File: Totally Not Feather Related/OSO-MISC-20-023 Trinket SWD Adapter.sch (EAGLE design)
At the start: 5 parts, among them X2 2x5 0.05" SWD

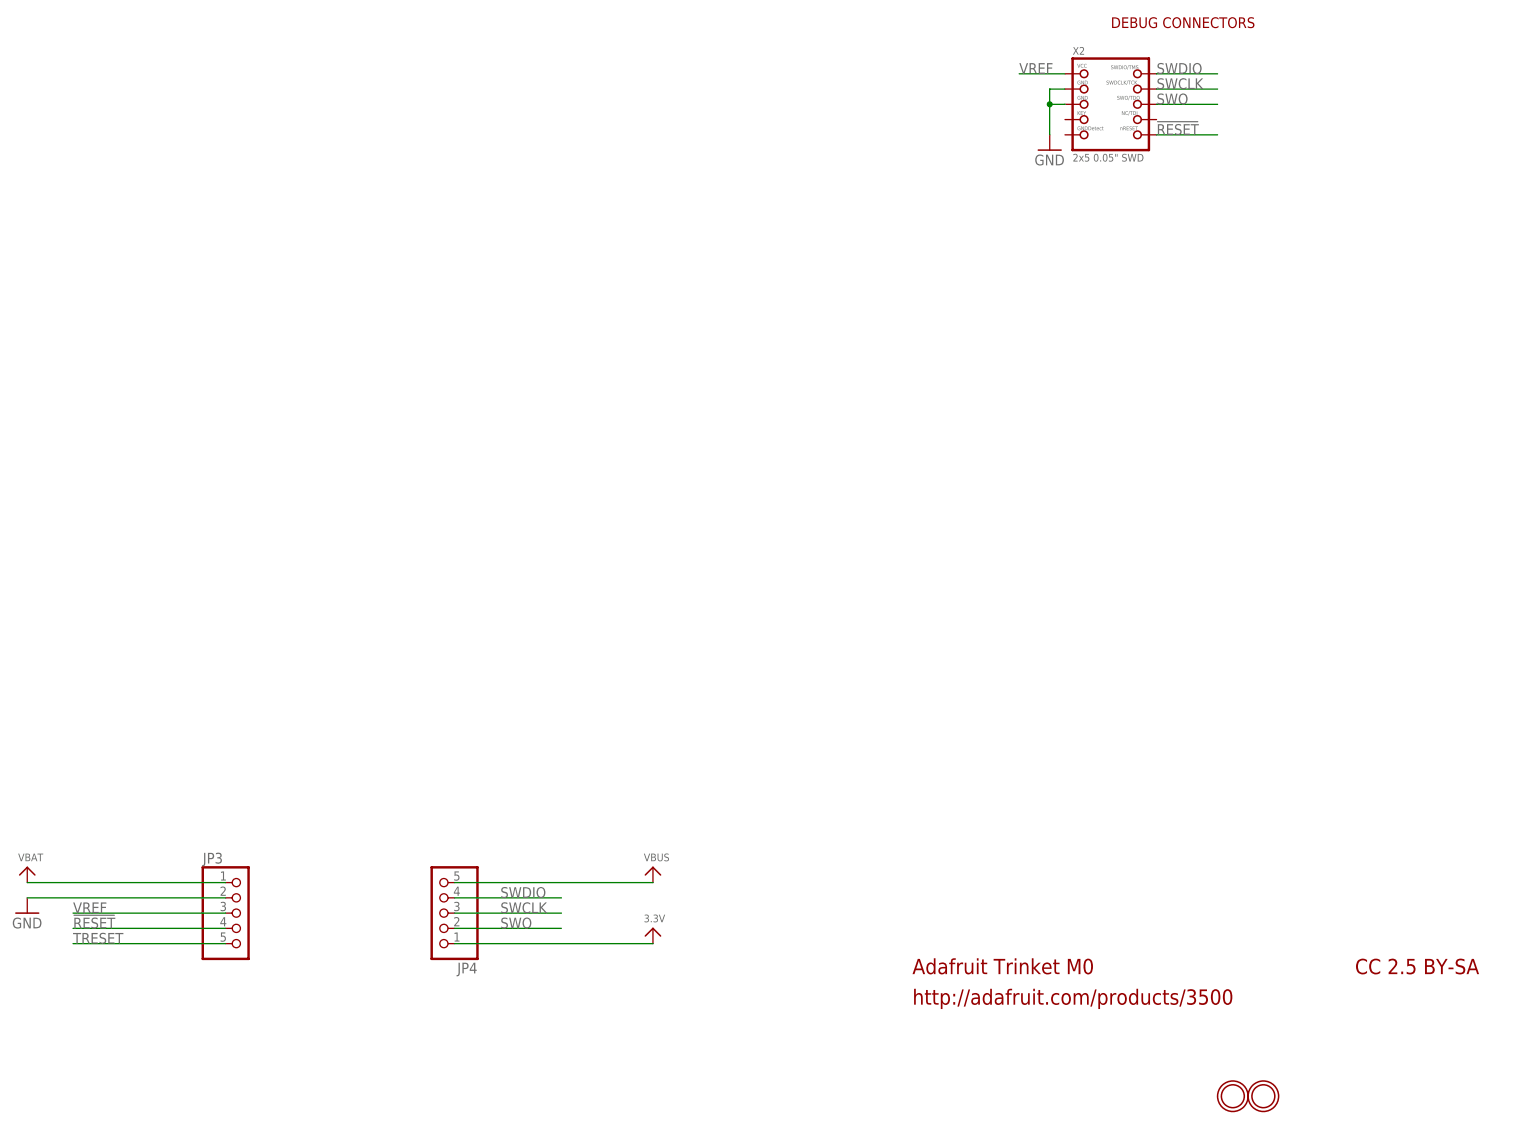
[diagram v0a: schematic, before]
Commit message: update trinket SWD adapter
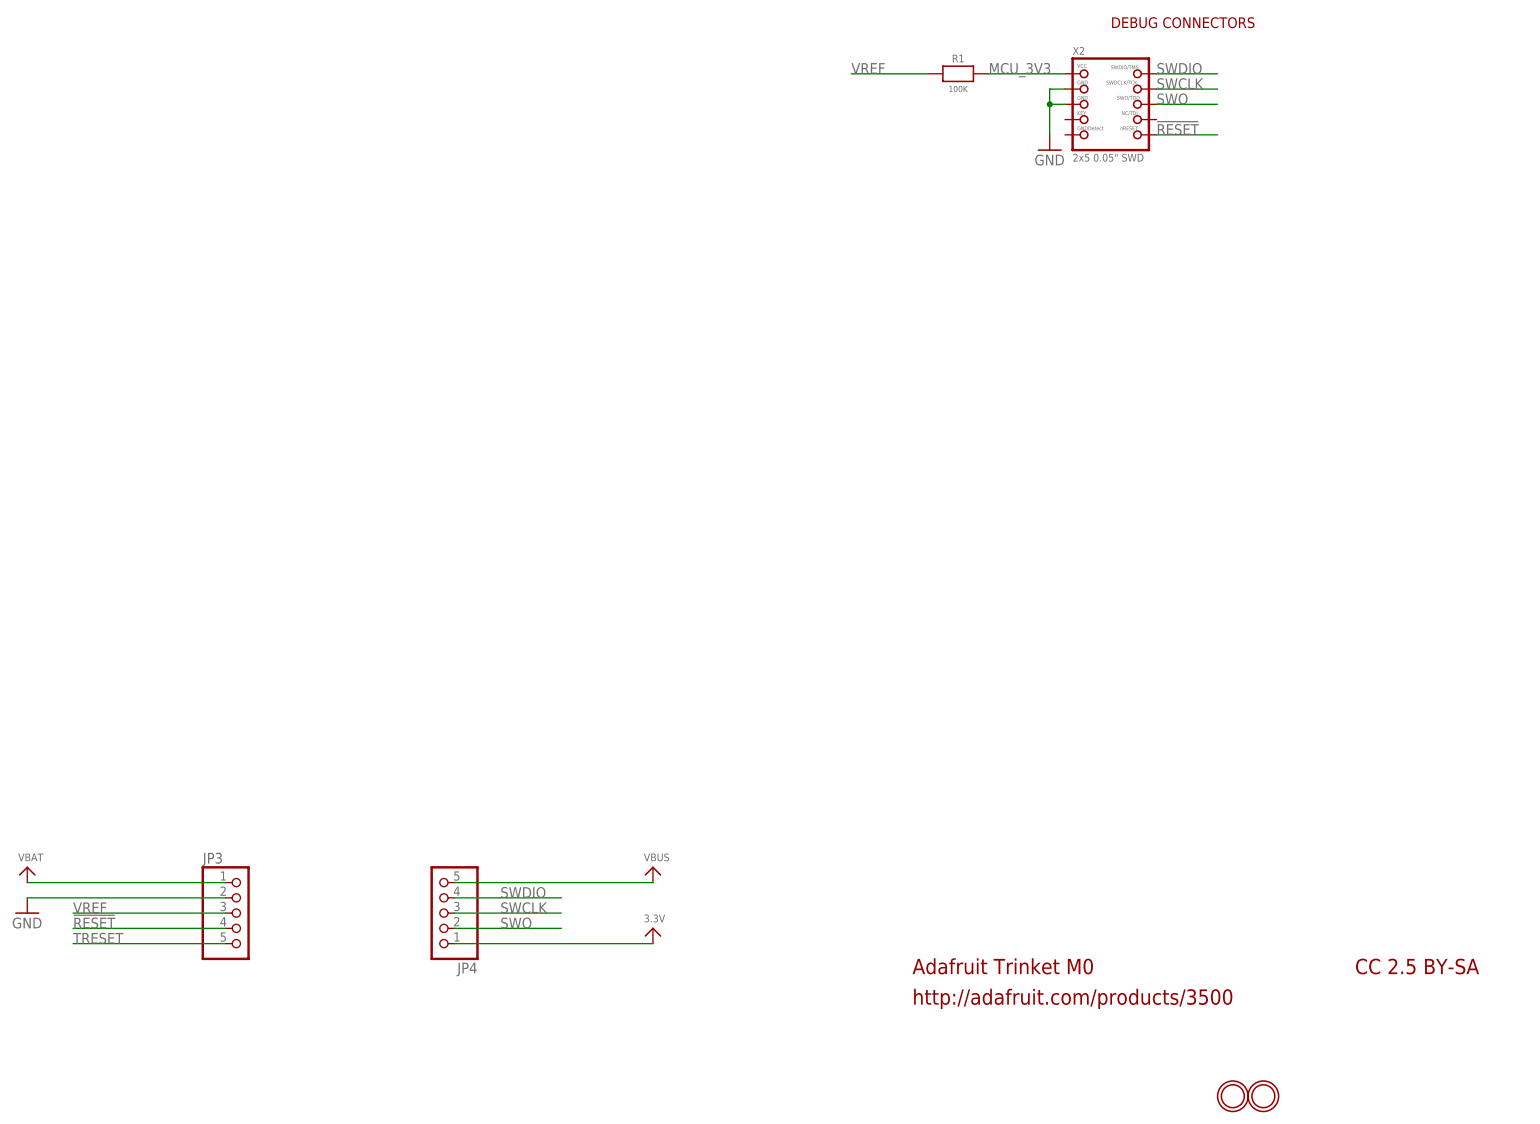
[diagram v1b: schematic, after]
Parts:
- added R1: 100K, microbuilder:RESISTOR0805_NOOUTLINE
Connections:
- new net MCU_3V3: R1.2, X2.VCC
- net VREF: now also R1.1; no longer X2.VCC
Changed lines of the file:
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@@
 <layer number="56" name="wert" color="7" fill="1" visible="no" active="no"/>
 <layer number="57" name="tCAD" color="7" fill="1" visible="no" active="no"/>
+<layer number="58" name="b3D" color="7" fill="1" visible="no" active="no"/>
 <layer number="59" name="tCarbon" color="7" fill="1" visible="no" active="no"/>
 <layer number="60" name="bCarbon" color="7" fill="1" visible="no" active="no"/>
+<layer number="61" name="stand" color="7" fill="1" visible="no" active="no"/>
 <layer number="88" name="SimResults" color="9" fill="1" visible="yes" active="yes"/>
 <layer number="89" name="SimProbes" color="9" fill="1" visible="yes" active="yes"/>
@@
 <part name="GND22" library="supply1" library_urn="urn:adsk.eagle:library:371" deviceset="GND" device=""/>
 <part name="X2" library="microbuilder" deviceset="JTAG-CORTEX" device="BOXPOSTS" value="2x5 0.05&quot; SWD"/>
+<part name="R1" library="microbuilder" deviceset="RESISTOR" device="0805_NOOUTLINE" value="100K"/>
 </parts>
 <sheets>
@@
 <attribute name="VALUE" x="201.93" y="165.735" size="1.27" layer="96"/>
 </instance>
+<instance part="R1" gate="G$1" x="182.88" y="180.34" smashed="yes">
+<attribute name="NAME" x="182.88" y="182.88" size="1.27" layer="95" font="vector" align="center"/>
+<attribute name="VALUE" x="182.88" y="177.8" size="1.016" layer="96" font="vector" ratio="15" align="center"/>
+</instance>
 </instances>
 <busses>
@@
 </segment>
 </net>
-<net name="VREF" class="1">
-<segment>
-<wire x1="193.04" y1="180.34" x2="200.66" y2="180.34" width="0.1524" layer="91"/>
+<net name="MCU_3V3" class="1">
+<segment>
+<wire x1="187.96" y1="180.34" x2="200.66" y2="180.34" width="0.1524" layer="91"/>
 <pinref part="X2" gate="G$1" pin="VCC"/>
-<label x="193.04" y="180.34" size="1.778" layer="95"/>
-</segment>
-<segment>
-<wire x1="60.96" y1="40.64" x2="35.56" y2="40.64" width="0.1524" layer="91"/>
-<label x="35.56" y="40.64" size="1.778" layer="95"/>
-<pinref part="JP3" gate="A" pin="3"/>
+<label x="187.96" y="180.34" size="1.778" layer="95"/>
+<pinref part="R1" gate="G$1" pin="2"/>
 </segment>
 </net>
@@
 </segment>
 </net>
+<net name="VREF" class="1">
+<segment>
+<label x="35.56" y="40.64" size="1.778" layer="95"/>
+<pinref part="JP3" gate="A" pin="3"/>
+<wire x1="35.56" y1="40.64" x2="60.96" y2="40.64" width="0.1524" layer="91"/>
+</segment>
+<segment>
+<label x="165.1" y="180.34" size="1.778" layer="95"/>
+<wire x1="165.1" y1="180.34" x2="177.8" y2="180.34" width="0.1524" layer="91"/>
+<pinref part="R1" gate="G$1" pin="1"/>
+</segment>
+</net>
